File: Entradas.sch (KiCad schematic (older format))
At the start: 22 parts, among them J11 TB_1X2, J12 TB_1X3-PonchoPLC-rescue, J8 TB_1X2, J9 TB_1X2, U9 SI8380P-IU

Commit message: version 3
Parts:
- JE1: renamed from J8; footprint TerminalBlock_Phoenix:TerminalBlock_Phoenix_MKDS-1,5-2_1x02_P5.00mm_Horizontal -> Poncho-PLC:TerminalBlock_4Ucon_1x02_P3.50mm_Horizontal
- JE2: renamed from J9; footprint TerminalBlock_Phoenix:TerminalBlock_Phoenix_MKDS-1,5-2_1x02_P5.00mm_Horizontal -> Poncho-PLC:TerminalBlock_4Ucon_1x02_P3.50mm_Horizontal
- JE3: renamed from J11; footprint TerminalBlock_Phoenix:TerminalBlock_Phoenix_MKDS-1,5-2_1x02_P5.00mm_Horizontal -> Poncho-PLC:TerminalBlock_4Ucon_1x02_P3.50mm_Horizontal
- JE4: renamed from J12; footprint TerminalBlock_Phoenix:TerminalBlock_Phoenix_MKDS-1,5-3_1x03_P5.00mm_Horizontal -> Poncho-PLC:TerminalBlock_4Ucon_1x03_P3.50mm_Horizontal
- U9: Digikey# 336-3618-5-ND -> (none)
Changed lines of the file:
@@
 $EndDescr
-$Comp
-L Silabs:SI8380P-IU U9
-U 1 1 5DFC34A6
-P 7300 3450
-F 0 "U9" H 7300 4365 50  0000 C CNN
-F 1 "SI8380P-IU" H 7300 4274 50  0000 C CNN
-F 2 "Package_SO:QSOP-20_3.9x8.7mm_P0.635mm" H 7250 3350 50  0001 C CNN
-F 3 "Si838x-DataSheet-1398003.pdf" H 7250 3350 50  0001 C CNN
-F 4 " 	336-3618-5-ND " H 7300 3450 50  0001 C CNN "Digikey#"
-	1    7300 3450
-	1    0    0    -1
-$EndComp
 $Comp
 L Poncho-PLC7-rescue:R-PonchoPLC-rescue R?
@@
 P 3850 3600
 AR Path="/5D85477B/5E049340" Ref="J?"  Part="1"
-AR Path="/5D8546B3/5E049340" Ref="J11"  Part="1"
-F 0 "J11" H 3650 3600 60  0000 C CNN
+AR Path="/5D8546B3/5E049340" Ref="JE3"  Part="1"
+F 0 "JE3" H 3650 3600 60  0000 C CNN
 F 1 "TB_1X2" H 3900 3300 60  0001 C CNN
-F 2 "TerminalBlock_Phoenix:TerminalBlock_Phoenix_MKDS-1,5-2_1x02_P5.00mm_Horizontal" H 3800 3650 60  0001 C CNN
+F 2 "Poncho-PLC:TerminalBlock_4Ucon_1x02_P3.50mm_Horizontal" H 3800 3650 60  0001 C CNN
 F 3 "1868733.pdf" H 3800 3650 60  0001 C CNN
 F 4 "" H 3850 3600 60  0001 C CNN "Title"
@@
 L Poncho-PLC7-rescue:TB_1X3-PonchoPLC-rescue J?
 U 1 1 5E049346
-P 3850 4000
+P 3850 4200
 AR Path="/5D85477B/5E049346" Ref="J?"  Part="1"
-AR Path="/5D8546B3/5E049346" Ref="J12"  Part="1"
-F 0 "J12" H 3720 3953 60  0000 R CNN
-F 1 "TB_1X3-PonchoPLC-rescue" H 3720 3847 60  0001 R CNN
-F 2 "TerminalBlock_Phoenix:TerminalBlock_Phoenix_MKDS-1,5-3_1x03_P5.00mm_Horizontal" H 3800 4050 60  0001 C CNN
-F 3 "1868733.pdf" H 3800 4050 60  0001 C CNN
-	1    3850 4000
-	1    0    0    -1
+AR Path="/5D8546B3/5E049346" Ref="JE4"  Part="1"
+F 0 "JE4" H 3720 4153 60  0000 R CNN
+F 1 "TB_1X3-PonchoPLC-rescue" H 3720 4047 60  0001 R CNN
+F 2 "Poncho-PLC:TerminalBlock_4Ucon_1x03_P3.50mm_Horizontal" H 3800 4250 60  0001 C CNN
+F 3 "1868733.pdf" H 3800 4250 60  0001 C CNN
+	1    3850 4200
+	1    0    0    1
 $EndComp
 $Comp
@@
 P 3850 3200
 AR Path="/5D85477B/5E057114" Ref="J?"  Part="1"
-AR Path="/5D8546B3/5E057114" Ref="J9"  Part="1"
-F 0 "J9" H 3650 3200 60  0000 C CNN
+AR Path="/5D8546B3/5E057114" Ref="JE2"  Part="1"
+F 0 "JE2" H 3650 3200 60  0000 C CNN
 F 1 "TB_1X2" H 3900 2900 60  0001 C CNN
-F 2 "TerminalBlock_Phoenix:TerminalBlock_Phoenix_MKDS-1,5-2_1x02_P5.00mm_Horizontal" H 3800 3250 60  0001 C CNN
+F 2 "Poncho-PLC:TerminalBlock_4Ucon_1x02_P3.50mm_Horizontal" H 3800 3250 60  0001 C CNN
 F 3 "1868733.pdf" H 3800 3250 60  0001 C CNN
 F 4 "" H 3850 3200 60  0001 C CNN "Title"
@@
 P 3850 2800
 AR Path="/5D85477B/5E05980D" Ref="J?"  Part="1"
-AR Path="/5D8546B3/5E05980D" Ref="J8"  Part="1"
-F 0 "J8" H 3650 2800 60  0000 C CNN
+AR Path="/5D8546B3/5E05980D" Ref="JE1"  Part="1"
+F 0 "JE1" H 3650 2800 60  0000 C CNN
 F 1 "TB_1X2" H 3900 2500 60  0001 C CNN
-F 2 "TerminalBlock_Phoenix:TerminalBlock_Phoenix_MKDS-1,5-2_1x02_P5.00mm_Horizontal" H 3800 2850 60  0001 C CNN
+F 2 "Poncho-PLC:TerminalBlock_4Ucon_1x02_P3.50mm_Horizontal" H 3800 2850 60  0001 C CNN
 F 3 "1868733.pdf" H 3800 2850 60  0001 C CNN
 F 4 "" H 3850 2800 60  0001 C CNN "Title"
@@
 Wire Wire Line
 	5350 5600 5350 5650
+$Comp
+L Silabs:SI8380P-IU U9
+U 1 1 5D9F834D
+P 7300 3450
+F 0 "U9" H 7300 4365 50  0000 C CNN
+F 1 "SI8380P-IU" H 7300 4274 50  0000 C CNN
+F 2 "Package_SO:QSOP-20_3.9x8.7mm_P0.635mm" H 7250 3350 50  0001 C CNN
+F 3 "Si838x-DataSheet-1398003.pdf" H 7250 3350 50  0001 C CNN
+	1    7300 3450
+	1    0    0    -1
+$EndComp
 $EndSCHEMATC

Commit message: Version 4
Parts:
- removed JE1, JE2, JE3: TB_1X2, Poncho-PLC:TerminalBlock_4Ucon_1x02_P3.50mm_Horizontal, symbol Poncho-PLC7-rescue:TB_1X2-PonchoPLC-rescue
- removed JE4: TB_1X3-PonchoPLC-rescue, Poncho-PLC:TerminalBlock_4Ucon_1x03_P3.50mm_Horizontal, symbol Poncho-PLC7-rescue:TB_1X3-PonchoPLC-rescue
- added JE1, JE2, JE3: TB_1X2, Poncho-PLC:TerminalBlock_WECO_120-M-311_1x02_P5.00mm_Plug-in_PCB, symbol Poncho-PLC7-rescue:TB_1X2
- added JE4: TB_1X3, Poncho-PLC:TerminalBlock_WECO_120-M-311_1x03_P5.00mm_Plug-in_PCB, symbol Poncho-PLC7-rescue:TB_1X3
- C9: symbol Poncho-PLC7-rescue:C_MINI-PonchoPLC-rescue -> Poncho-PLC7-rescue:C_MINI; Desc (none) -> 0.1µF ±10% 50V Ceramic Capacitor X7R 1206 (3216 Metric); Digikey# 1276-1007-2-ND -> CL31B104KBCNNNL-ND
- R17, R19, R21, R23, R25, R27, R29, R31: value 6200 -> 6.2K; symbol Poncho-PLC7-rescue:R-PonchoPLC-rescue -> Poncho-PLC7-rescue:R; Desc (none) -> 1/8W Chip Resistor 0805; Digikey# (none) -> CR0805-JW-622ELFTR-ND; Manf (none) -> CR0805-JW-622ELFTR-ND
- R18, R20, R22, R24, R26, R28, R30, R32: value 2700 -> 2.7K; symbol Poncho-PLC7-rescue:R-PonchoPLC-rescue -> Poncho-PLC7-rescue:R; Desc (none) -> 1/8W Chip Resistor 0805; Digikey# (none) -> CR0805-JW-272ELFTR-ND
- U9: symbol Silabs:SI8380P-IU -> Poncho-PLC7-rescue:SI8380P-IU; Desc (none) -> General Purpose Digital Isolator 2500Vrms 8 Channel 2Mbps 2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; Digikey# (none) -> 336-3618-5-ND
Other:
- note added: "ENTRADAS DIGITALES AISLADAS\n"
- note removed: "ISOLATED DIGITAL INPUTS\n"
- moved on the sheet: U9

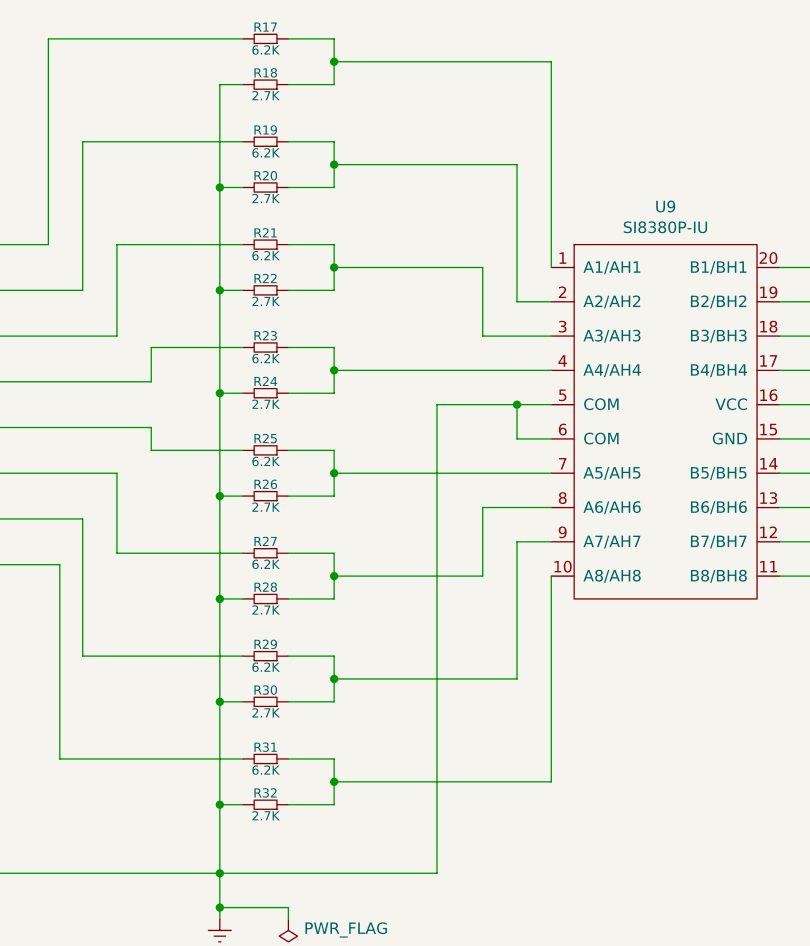
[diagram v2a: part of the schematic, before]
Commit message: Ruteo Parcial-Replanteo Esquematico pafa favorecer ruteo
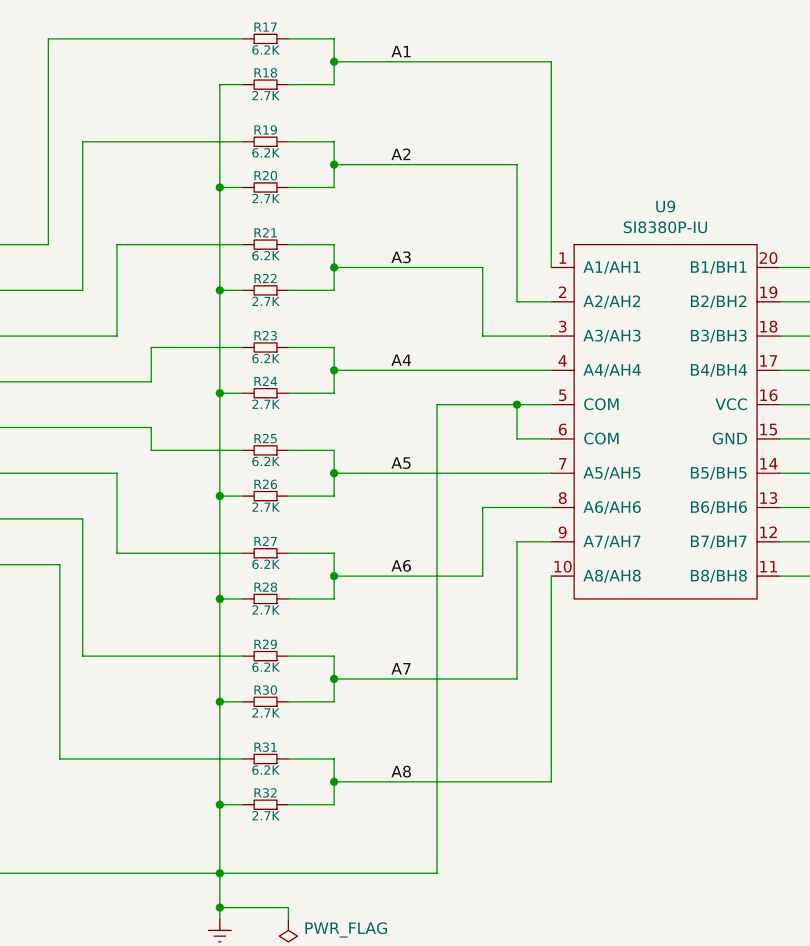
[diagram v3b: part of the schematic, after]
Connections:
- net A1: now reaches R17.1, R18.1, U9.1 (A1/AH1)
- net A8: now reaches R31.1, R32.1, U9.10 (A8/AH8)
- net A2: now reaches R19.1, R20.1, U9.2 (A2/AH2)
- net A3: now reaches R21.1, R22.1, U9.3 (A3/AH3)
- net A4: now reaches R23.1, R24.1, U9.4 (A4/AH4)
- net A5: now reaches R25.1, R26.1, U9.7 (A5/AH5)
- net A6: now reaches R27.1, R28.1, U9.8 (A6/AH6)
- net A7: now reaches R29.1, R30.1, U9.9 (A7/AH7)
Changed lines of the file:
@@
 	1    0    0    1
 $EndComp
+Text Label 6300 1250 0    50   ~ 0
+A1
+Text Label 6300 1700 0    50   ~ 0
+A2
+Text Label 6300 2150 0    50   ~ 0
+A3
+Text Label 6300 2600 0    50   ~ 0
+A4
+Text Label 6300 3050 0    50   ~ 0
+A5
+Text Label 6300 3500 0    50   ~ 0
+A6
+Text Label 6300 3950 0    50   ~ 0
+A7
+Text Label 6300 4400 0    50   ~ 0
+A8
 $EndSCHEMATC
